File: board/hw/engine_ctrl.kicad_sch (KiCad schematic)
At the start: 0 parts

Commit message: * moved potentiometer to engine's sheet * added engine's Vcc feedback
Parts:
- added R4, R5: 100k, Resistor_SMD:R_0603_1608Metric, symbol Device:R
- added RV1: CDE23N-60-B50K, st_passives_potentiometers:CDE23N-60-B50K, symbol Device:R_Potentiometer
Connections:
- new net +12V: R4.1
- new net +3.3V: RV1.1
- new net GND: R5.2, RV1.3
- new net eng_Vcc_feedback: R4.2, R5.1
- new net eng_pos_feedback: RV1.2
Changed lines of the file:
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@@
 (kicad_sch (version 20230121) (generator eeschema)
   (paper "A4")
+  (junction (at 52.07 100.965) (diameter 0) (color 0 0 0 0)
+  )
+  (wire (pts (xy 52.07 99.06) (xy 52.07 100.965))
+    (stroke (width 0) (type default))
+  )
+  (wire (pts (xy 47.625 100.965) (xy 52.07 100.965))
+    (stroke (width 0) (type default))
+  )
+  (wire (pts (xy 52.07 100.965) (xy 52.07 102.87))
+    (stroke (width 0) (type default))
+  )
+  (wire (pts (xy 76.2 135.255) (xy 76.2 136.525))
+    (stroke (width 0) (type default))
+  )
+  (wire (pts (xy 83.185 140.335) (xy 80.01 140.335))
+    (stroke (width 0) (type default))
+  )
+  (wire (pts (xy 76.2 144.145) (xy 76.2 145.415))
+    (stroke (width 0) (type default))
+  )
+  (hierarchical_label "eng_Vcc_feedback" (shape output) (at 47.625 100.965 180) (fields_autoplaced)
+    (effects (font (size 1.27 1.27)) (justify right))
+  )
+  (hierarchical_label "eng_pos_feedback" (shape output) (at 83.185 140.335 0) (fields_autoplaced)
+    (effects (font (size 1.27 1.27)) (justify left))
+  )
+  (symbol (lib_id "power:GND") (at 76.2 145.415 0) (unit 1)
+    (in_bom yes) (on_board yes) (dnp no) (fields_autoplaced)
+    (property "Reference" "#PWR07" (at 76.2 151.765 0)
+      (effects (font (size 1.27 1.27)) hide)
+    )
+    (property "Value" "GND" (at 76.2 150.495 0)
+      (effects (font (size 1.27 1.27)))
+    )
+    (property "Footprint" "" (at 76.2 145.415 0)
+      (effects (font (size 1.27 1.27)) hide)
+    )
+    (property "Datasheet" "" (at 76.2 145.415 0)
+      (effects (font (size 1.27 1.27)) hide)
+    )
+    (pin "1")
+    (instances
+      (project "yals"
+        (path "/920838ab-42d6-4f6a-a4ed-bf4606dd42d5/e7d03af2-c113-440c-81a4-7c3f8aeef75a"
+          (reference "#PWR07") (unit 1)
+        )
+      )
+    )
+  )
+  (symbol (lib_id "Device:R") (at 52.07 106.68 0) (unit 1)
+    (in_bom yes) (on_board yes) (dnp no) (fields_autoplaced)
+    (property "Reference" "R5" (at 54.61 105.41 0)
+      (effects (font (size 1.27 1.27)) (justify left))
+    )
+    (property "Value" "100k" (at 54.61 107.95 0)
+      (effects (font (size 1.27 1.27)) (justify left))
+    )
+    (property "Footprint" "Resistor_SMD:R_0603_1608Metric" (at 50.292 106.68 90)
+      (effects (font (size 1.27 1.27)) hide)
+    )
+    (property "Datasheet" "~" (at 52.07 106.68 0)
+      (effects (font (size 1.27 1.27)) hide)
+    )
+    (pin "1")
+    (pin "2")
+    (instances
+      (project "yals"
+        (path "/920838ab-42d6-4f6a-a4ed-bf4606dd42d5/e7d03af2-c113-440c-81a4-7c3f8aeef75a"
+          (reference "R5") (unit 1)
+        )
+      )
+    )
+  )
+  (symbol (lib_id "Device:R_Potentiometer") (at 76.2 140.335 0) (unit 1)
+    (in_bom yes) (on_board yes) (dnp no) (fields_autoplaced)
+    (property "Reference" "RV1" (at 73.66 139.065 0)
+      (effects (font (size 1.27 1.27)) (justify right))
+    )
+    (property "Value" "CDE23N-60-B50K" (at 73.66 141.605 0)
+      (effects (font (size 1.27 1.27)) (justify right))
+    )
+    (property "Footprint" "st_passives_potentiometers:CDE23N-60-B50K" (at 76.2 140.335 0)
+      (effects (font (size 1.27 1.27)) hide)
+    )
+    (property "Datasheet" "~" (at 76.2 140.335 0)
+      (effects (font (size 1.27 1.27)) hide)
+    )
+    (pin "1")
+    (pin "3")
+    (pin "2")
+    (instances
+      (project "yals"
+        (path "/920838ab-42d6-4f6a-a4ed-bf4606dd42d5/e7d03af2-c113-440c-81a4-7c3f8aeef75a"
+          (reference "RV1") (unit 1)
+        )
+      )
+    )
+  )
+  (symbol (lib_id "power:GND") (at 52.07 110.49 0) (unit 1)
+    (in_bom yes) (on_board yes) (dnp no) (fields_autoplaced)
+    (property "Reference" "#PWR038" (at 52.07 116.84 0)
+      (effects (font (size 1.27 1.27)) hide)
+    )
+    (property "Value" "GND" (at 52.07 115.57 0)
+      (effects (font (size 1.27 1.27)))
+    )
+    (property "Footprint" "" (at 52.07 110.49 0)
+      (effects (font (size 1.27 1.27)) hide)
+    )
+    (property "Datasheet" "" (at 52.07 110.49 0)
+      (effects (font (size 1.27 1.27)) hide)
+    )
+    (pin "1")
+    (instances
+      (project "yals"
+        (path "/920838ab-42d6-4f6a-a4ed-bf4606dd42d5/e7d03af2-c113-440c-81a4-7c3f8aeef75a"
+          (reference "#PWR038") (unit 1)
+        )
+      )
+    )
+  )
+  (symbol (lib_id "power:+12V") (at 52.07 91.44 0) (unit 1)
+    (in_bom yes) (on_board yes) (dnp no) (fields_autoplaced)
+    (property "Reference" "#PWR039" (at 52.07 95.25 0)
+      (effects (font (size 1.27 1.27)) hide)
+    )
+    (property "Value" "+12V" (at 52.07 86.36 0)
+      (effects (font (size 1.27 1.27)))
+    )
+    (property "Footprint" "" (at 52.07 91.44 0)
+      (effects (font (size 1.27 1.27)) hide)
+    )
+    (property "Datasheet" "" (at 52.07 91.44 0)
+      (effects (font (size 1.27 1.27)) hide)
+    )
+    (pin "1")
+    (instances
+      (project "yals"
+        (path "/920838ab-42d6-4f6a-a4ed-bf4606dd42d5/e7d03af2-c113-440c-81a4-7c3f8aeef75a"
+          (reference "#PWR039") (unit 1)
+        )
+      )
+    )
+  )
+  (symbol (lib_id "Device:R") (at 52.07 95.25 0) (unit 1)
+    (in_bom yes) (on_board yes) (dnp no) (fields_autoplaced)
+    (property "Reference" "R4" (at 54.61 93.98 0)
+      (effects (font (size 1.27 1.27)) (justify left))
+    )
+    (property "Value" "100k" (at 54.61 96.52 0)
+      (effects (font (size 1.27 1.27)) (justify left))
+    )
+    (property "Footprint" "Resistor_SMD:R_0603_1608Metric" (at 50.292 95.25 90)
+      (effects (font (size 1.27 1.27)) hide)
+    )
+    (property "Datasheet" "~" (at 52.07 95.25 0)
+      (effects (font (size 1.27 1.27)) hide)
+    )
+    (pin "1")
+    (pin "2")
+    (instances
+      (project "yals"
+        (path "/920838ab-42d6-4f6a-a4ed-bf4606dd42d5/e7d03af2-c113-440c-81a4-7c3f8aeef75a"
+          (reference "R4") (unit 1)
+        )
+      )
+    )
+  )
+  (symbol (lib_id "power:+3.3V") (at 76.2 135.255 0) (unit 1)
+    (in_bom yes) (on_board yes) (dnp no) (fields_autoplaced)
+    (property "Reference" "#PWR06" (at 76.2 139.065 0)
+      (effects (font (size 1.27 1.27)) hide)
+    )
+    (property "Value" "+3.3V" (at 76.2 130.175 0)
+      (effects (font (size 1.27 1.27)))
+    )
+    (property "Footprint" "" (at 76.2 135.255 0)
+      (effects (font (size 1.27 1.27)) hide)
+    )
+    (property "Datasheet" "" (at 76.2 135.255 0)
+      (effects (font (size 1.27 1.27)) hide)
+    )
+    (pin "1")
+    (instances
+      (project "yals"
+        (path "/920838ab-42d6-4f6a-a4ed-bf4606dd42d5/e7d03af2-c113-440c-81a4-7c3f8aeef75a"
+          (reference "#PWR06") (unit 1)
+        )
+      )
+    )
+  )
 )

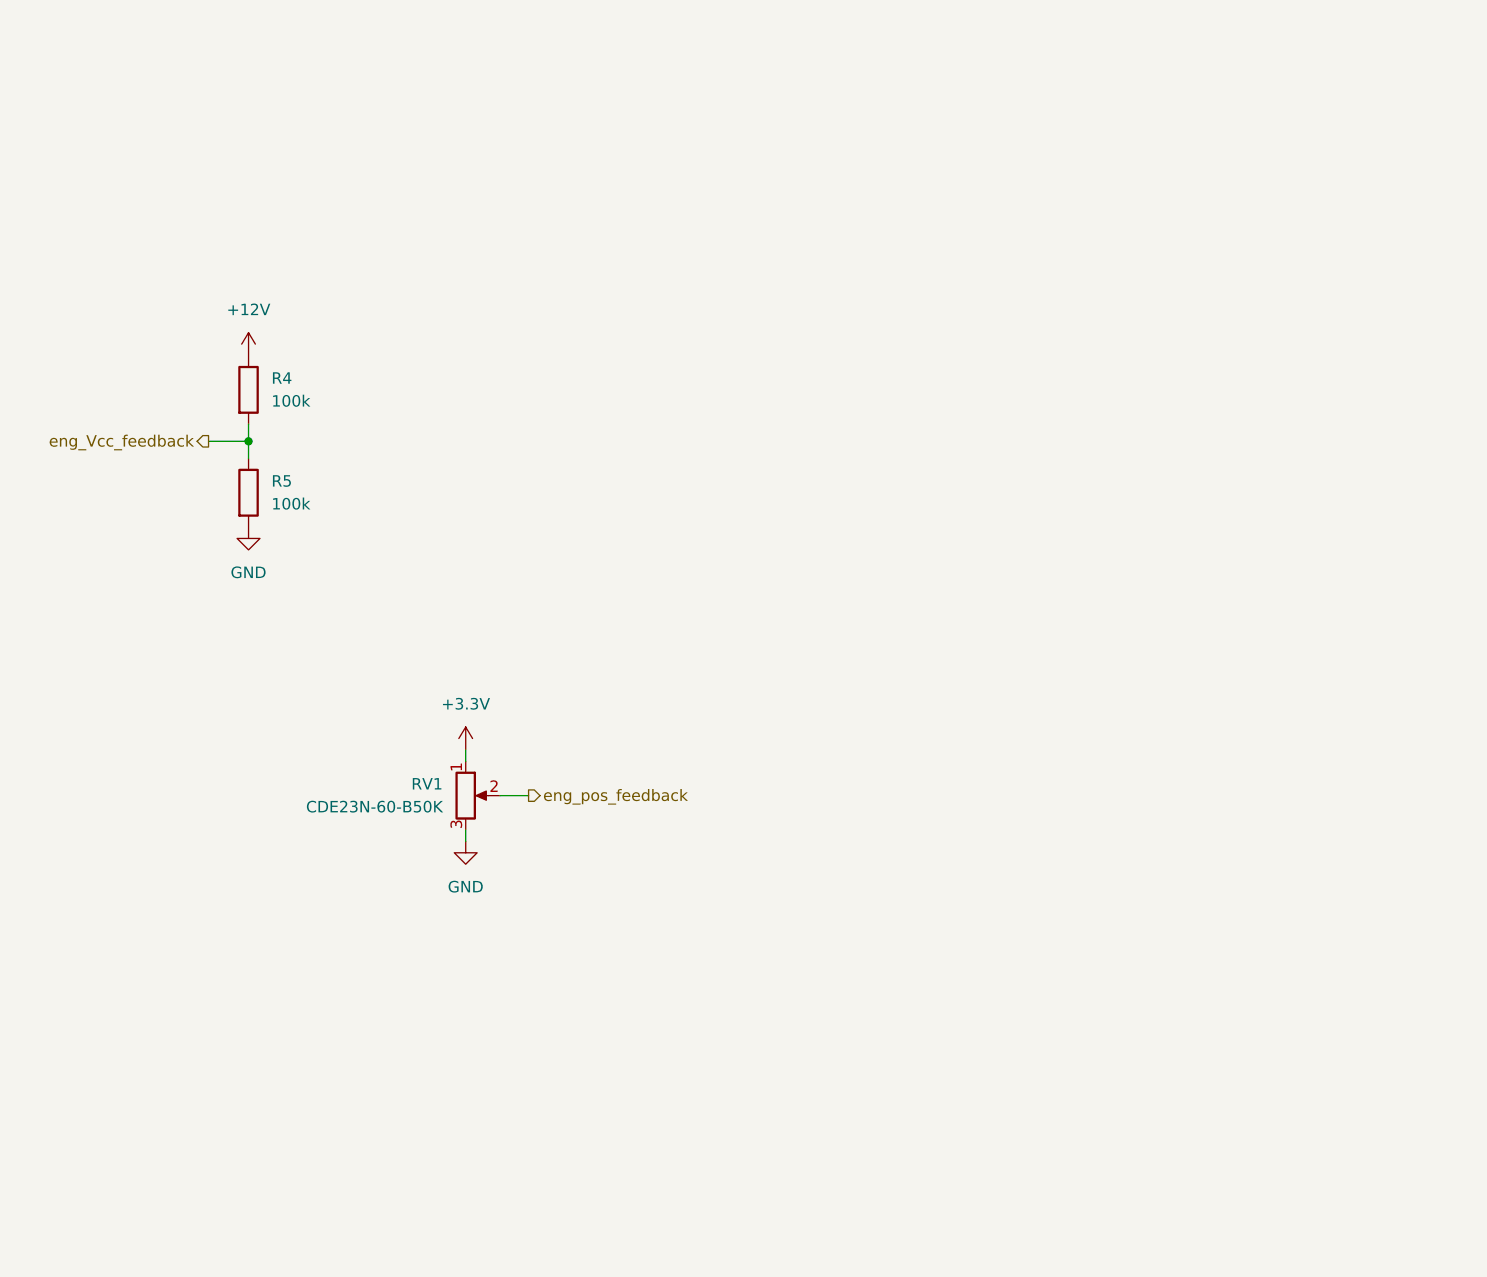
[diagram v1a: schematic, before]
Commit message: added engine driver with votage measuring resistor to schematics
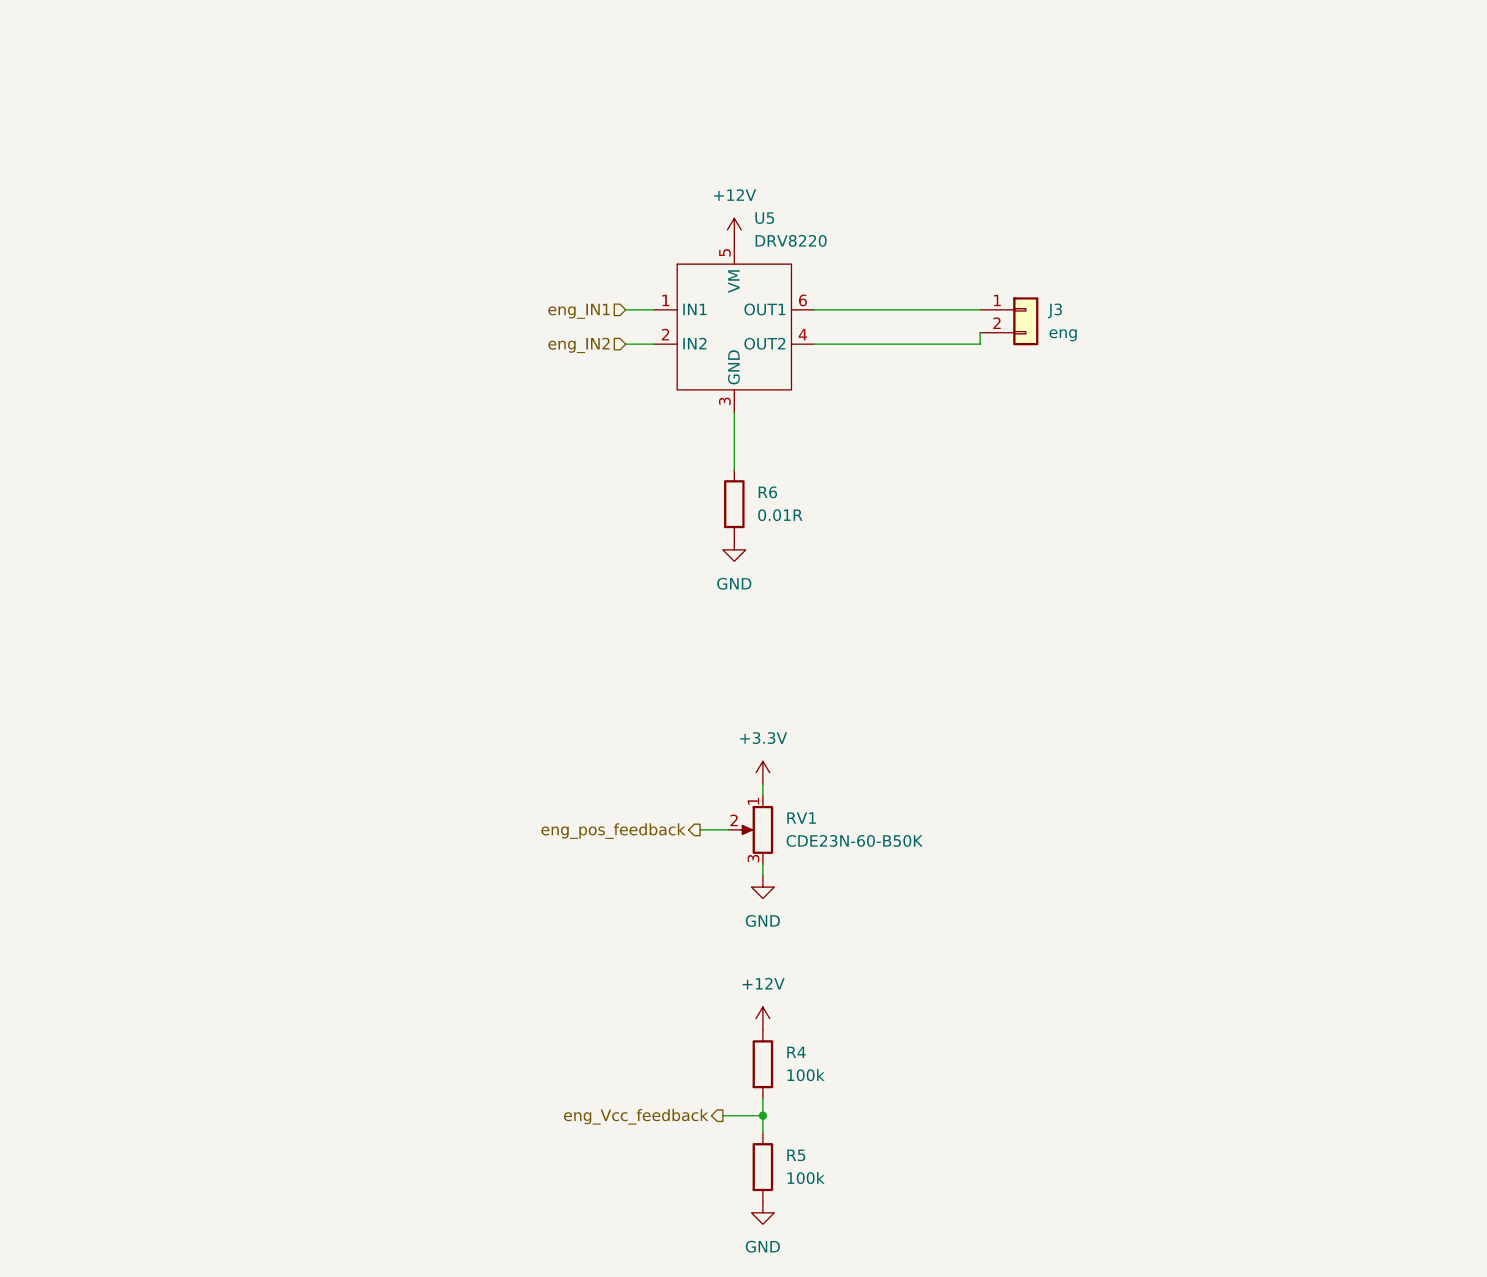
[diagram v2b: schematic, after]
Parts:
- added J3: eng, Connector_PinHeader_2.54mm:PinHeader_1x02_P2.54mm_Vertical, symbol Connector_Generic:Conn_01x02
- added R6: 0.01R, Resistor_SMD:R_1206_3216Metric, symbol Device:R
- added U5: DRV8220, Package_TO_SOT_SMD:SOT-563, symbol ti_eng_driver:DRV8220
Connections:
- net +12V: now also U5.5 (VM)
- net GND: now also R6.2
- new net: R6.1, U5.3 (GND)
- new net: J3.2 (Pin_2), U5.4 (OUT2)
- new net: J3.1 (Pin_1), U5.6 (OUT1)
- new net eng_IN1: U5.1 (IN1)
- new net eng_IN2: U5.2 (IN2)
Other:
- moved on the sheet: R4, R5, RV1

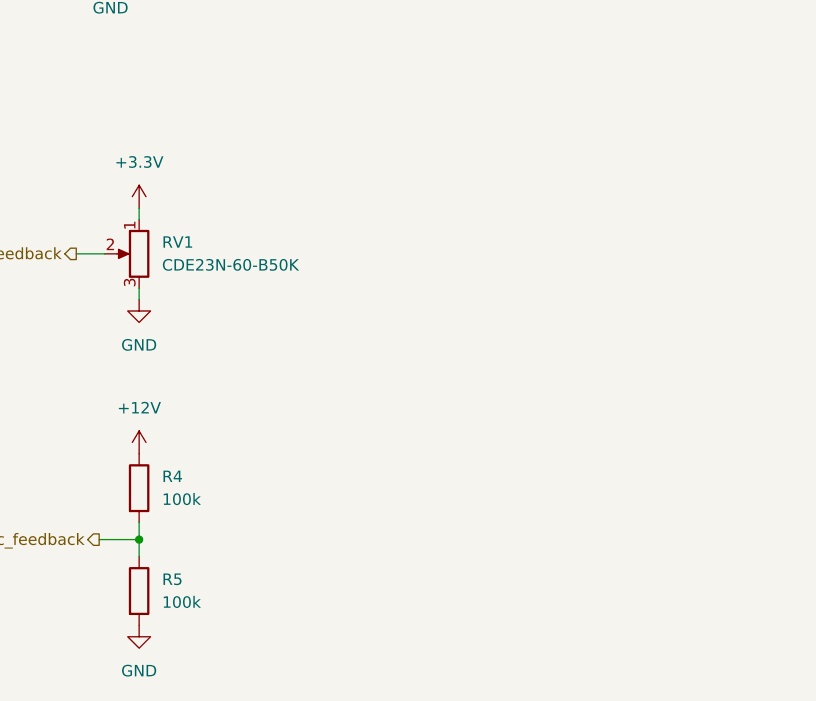
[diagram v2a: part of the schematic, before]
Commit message: voltage measuing capacity has been added
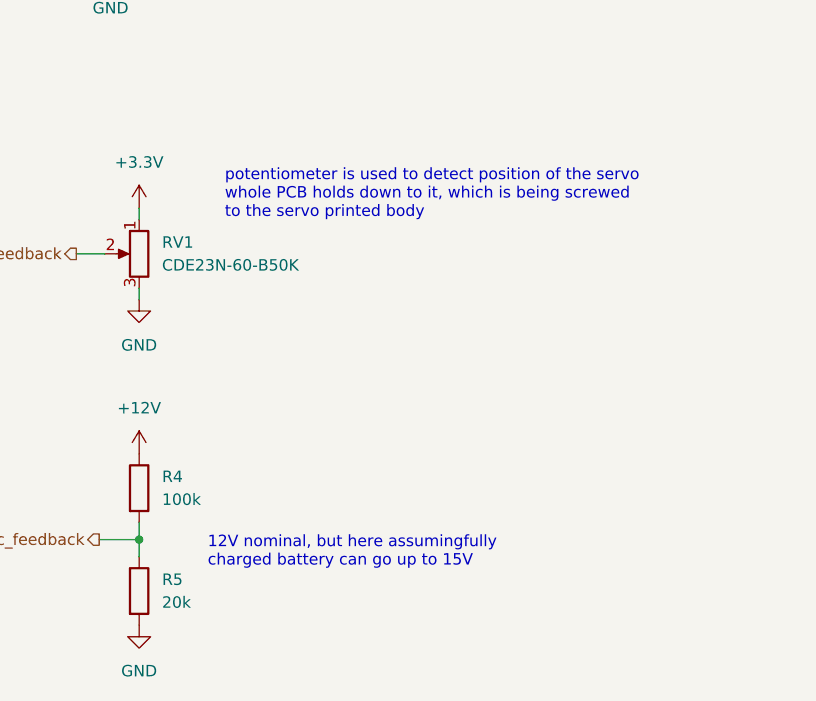
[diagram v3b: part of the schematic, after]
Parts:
- R5: value 100k -> 20k
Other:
- note added: "12V nominal, but here assumingfully charged battery can go up to 15V"
- note added: "potentiometer is used to detect position of the servo whole PCB holds down to it, which is being screwed to the servo printed body"
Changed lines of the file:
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@@
     (stroke (width 0) (type default))
+  )
+  (text "12V nominal, but here assumingfully\ncharged battery can go up to 15V"
+    (at 116.84 179.07 0)
+    (effects (font (size 1.27 1.27)) (justify left bottom))
+  )
+  (text "potentiometer is used to detect position of the servo\nwhole PCB holds down to it, which is being screwed\nto the servo printed body"
+    (at 118.745 140.335 0)
+    (effects (font (size 1.27 1.27)) (justify left bottom))
   )
   (hierarchical_label "eng_IN2" (shape input) (at 93.98 90.17 180) (fields_autoplaced)
@@
       (effects (font (size 1.27 1.27)) (justify left))
     )
-    (property "Value" "100k" (at 111.76 182.88 0)
+    (property "Value" "20k" (at 111.76 182.88 0)
       (effects (font (size 1.27 1.27)) (justify left))
     )
